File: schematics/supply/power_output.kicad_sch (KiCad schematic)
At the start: 39 parts, among them Q10 IRLML5203, U2 EL817, U22 TL331, U23 INA228, U9 IRS2153S

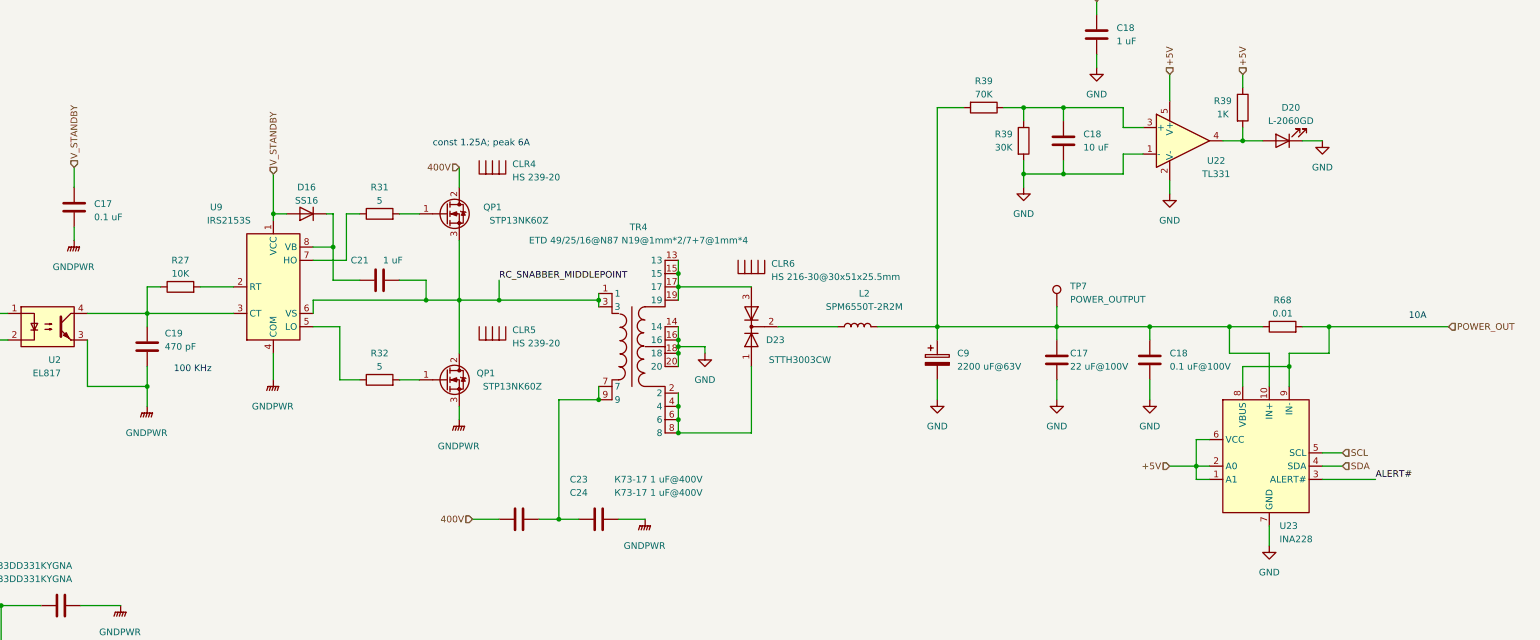
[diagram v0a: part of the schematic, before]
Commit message: prepare to replace ina228 to attiny16+ina169(?). ina228 is an intresting chip, but its too expensive and Im not sure I can buy it on ali
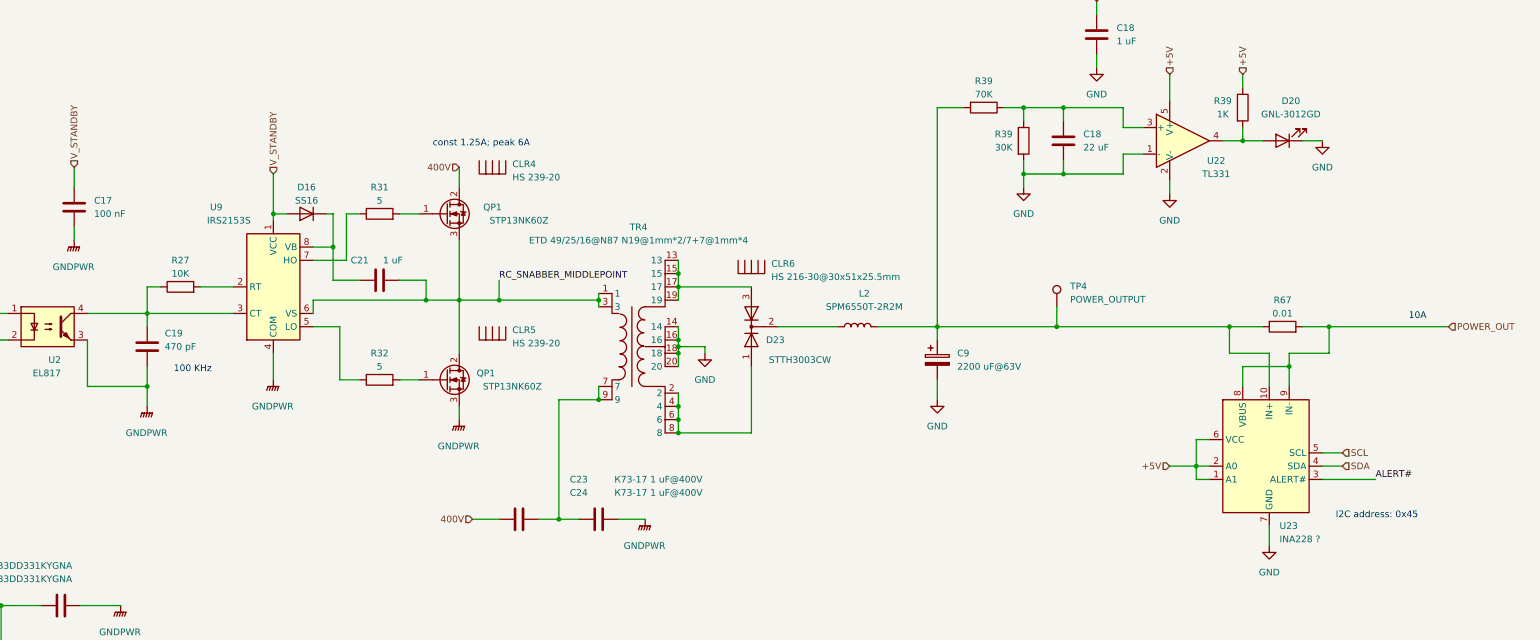
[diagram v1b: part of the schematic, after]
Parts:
- removed C17: 22 uF@100V, Capacitor_SMD:C_1210_3225Metric, symbol Device:C
- removed C18: 0.1 uF@100V, Capacitor_SMD:C_0603_1608Metric, symbol Device:C
- C17: value 0.1 uF -> 100 nF
- C18: value 10 uF -> 22 uF; footprint Capacitor_SMD:C_0603_1608Metric -> Capacitor_SMD:C_1210_3225Metric
- C23, C24: footprint Capacitor_THT:C_Rect_L31.5mm_W9.0mm_P27.50mm_MKS4 -> Capacitor_THT:C_Rect_L24.0mm_W12.8mm_P22.50mm_MKT
- D20: value L-2060GD -> GNL-3012GD
- U23: value INA228 -> INA228 ?
- renumbered R68 to R67, TP7 to TP4
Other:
- note added: "I2C address: 0x45"

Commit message: Prepare to move USB ports to a few millimenters outside
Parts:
- removed Q10 (x2): IRLML5203, Package_TO_SOT_SMD:SOT-23, symbol Transistor_FET:IRLML5203
- removed R27: 10K, Resistor_SMD:R_0805_2012Metric, symbol Device:R
- removed U23: INA228 ?, Package_SO:VSSOP-10_3x3mm_P0.5mm, symbol My_Library:INA228
- added C18 (x2): 10 nF, Capacitor_SMD:C_0603_1608Metric, symbol Device:C
- added C18: 1 uF, Capacitor_SMD:C_0603_1608Metric, symbol Device:C
- added Q10: IRLML0030, Package_TO_SOT_SMD:SOT-23, symbol Transistor_FET:IRLML0030
- added R70: 9K1, Resistor_SMD:R_0805_2012Metric, symbol Device:R
- added R71: 1K, Resistor_SMD:R_0805_2012Metric, symbol Device:R
- added R74: 49K5, Resistor_SMD:R_0805_2012Metric, symbol Device:R
- added U24: INA169, Package_TO_SOT_SMD:SOT-23-5, symbol Amplifier_Current:INA169
- R73: renamed from R67; footprint Resistor_SMD:R_1206_3216Metric -> Resistor_SMD:R_2512_6332Metric
- renumbered D20 to D23, U22 to U23
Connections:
- net +5V: now also R18.1, C18.2, U24.5 (V+)
- net GND: now also C18.1, C18.1, C18.1, Q10.2 (S), R71.1, R74.1, U24.2 (GND); no longer R18.1
- net POWER_OUT: now also U24.4 (-)
- net at R18.2: now also U2.1; no longer U2.2
- net at C9.1, L2.2, R39.2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: now also R70.2, U24.3 (+)
- new net: Q10.3 (D), U2.2
- new net POWER_OUTPUT_CURRENT_SENSE: C18.2, R74.2, U24.1
- new net POWER_OUTPUT_FB: Q10.1 (G)
- new net POWER_OUTPUT_VOLT_SENSE: C18.2, R70.1, R71.2
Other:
- note removed: "I2C address: 0x45"
- moved on the sheet: R18, R73

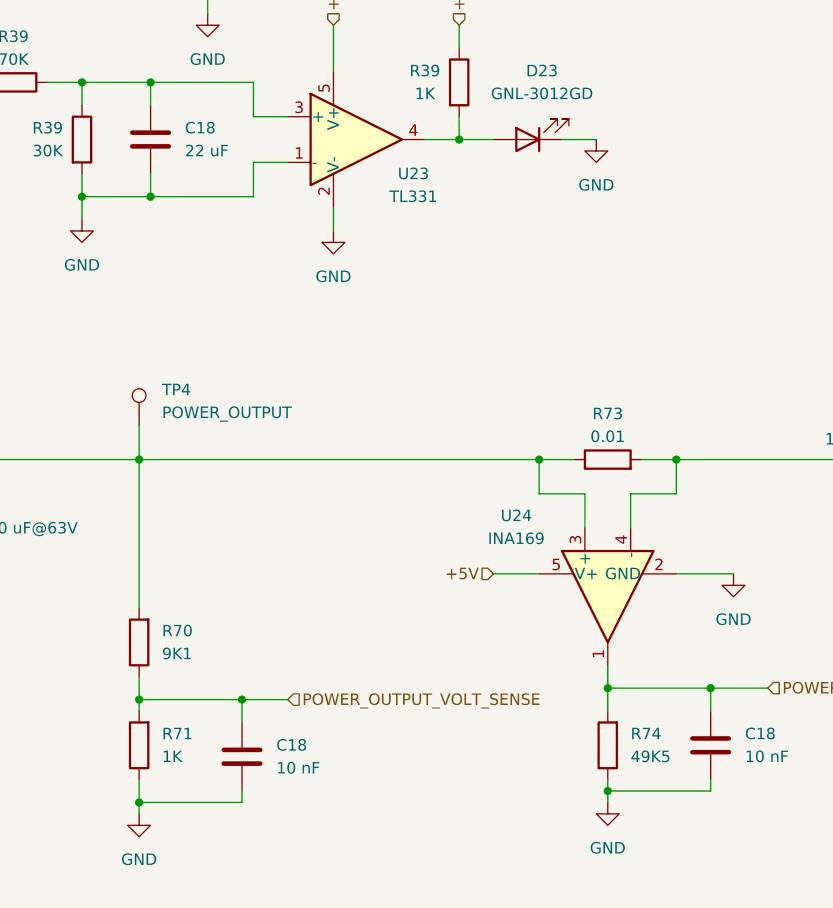
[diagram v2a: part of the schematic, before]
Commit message: little changes in schematics
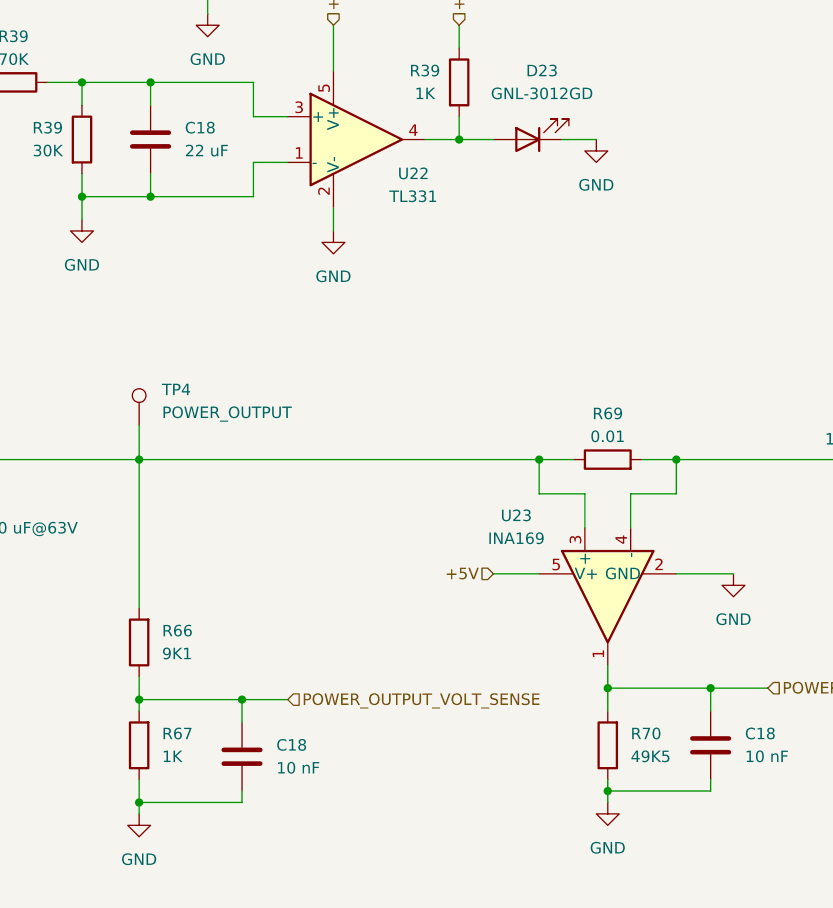
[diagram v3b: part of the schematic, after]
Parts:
- renumbered R70 to R66, R71 to R67, R73 to R69, R74 to R70, U23 to U22, U24 to U23

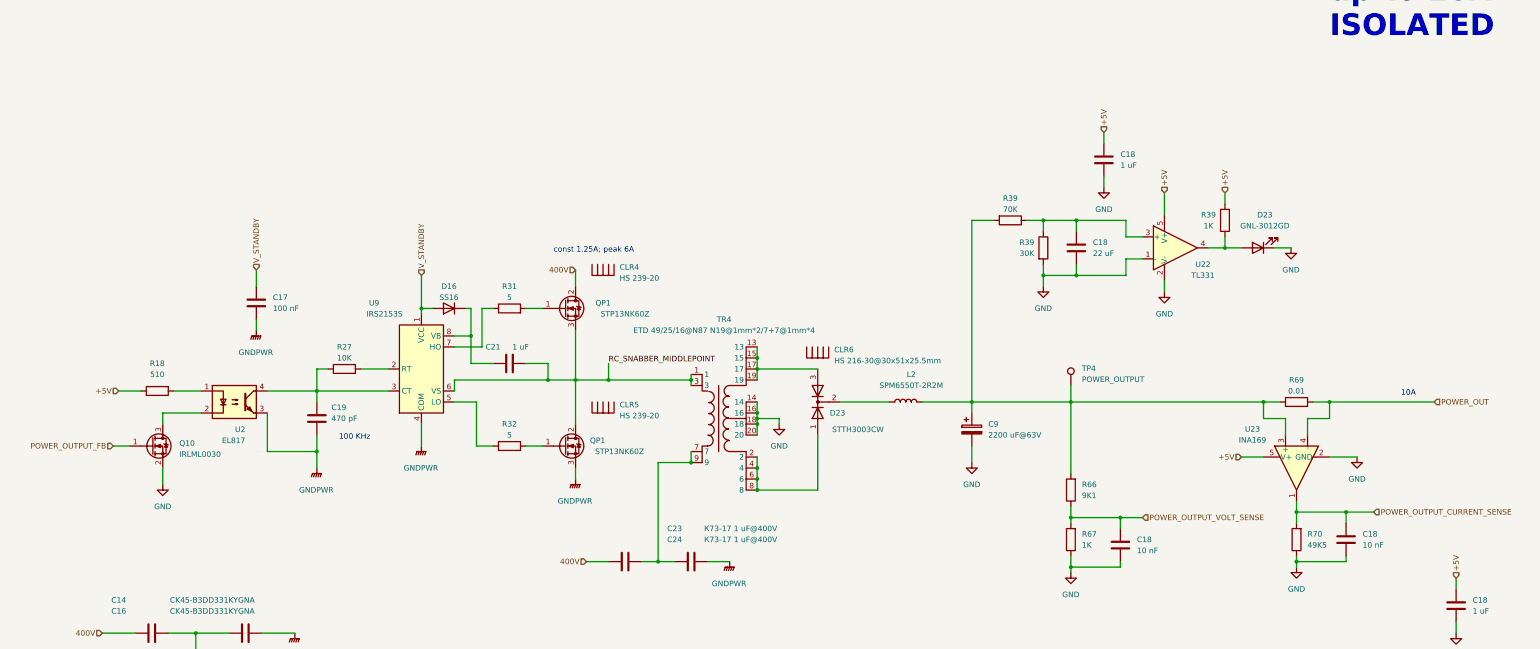
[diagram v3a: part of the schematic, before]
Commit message: Added over-voltage protection to 5V line
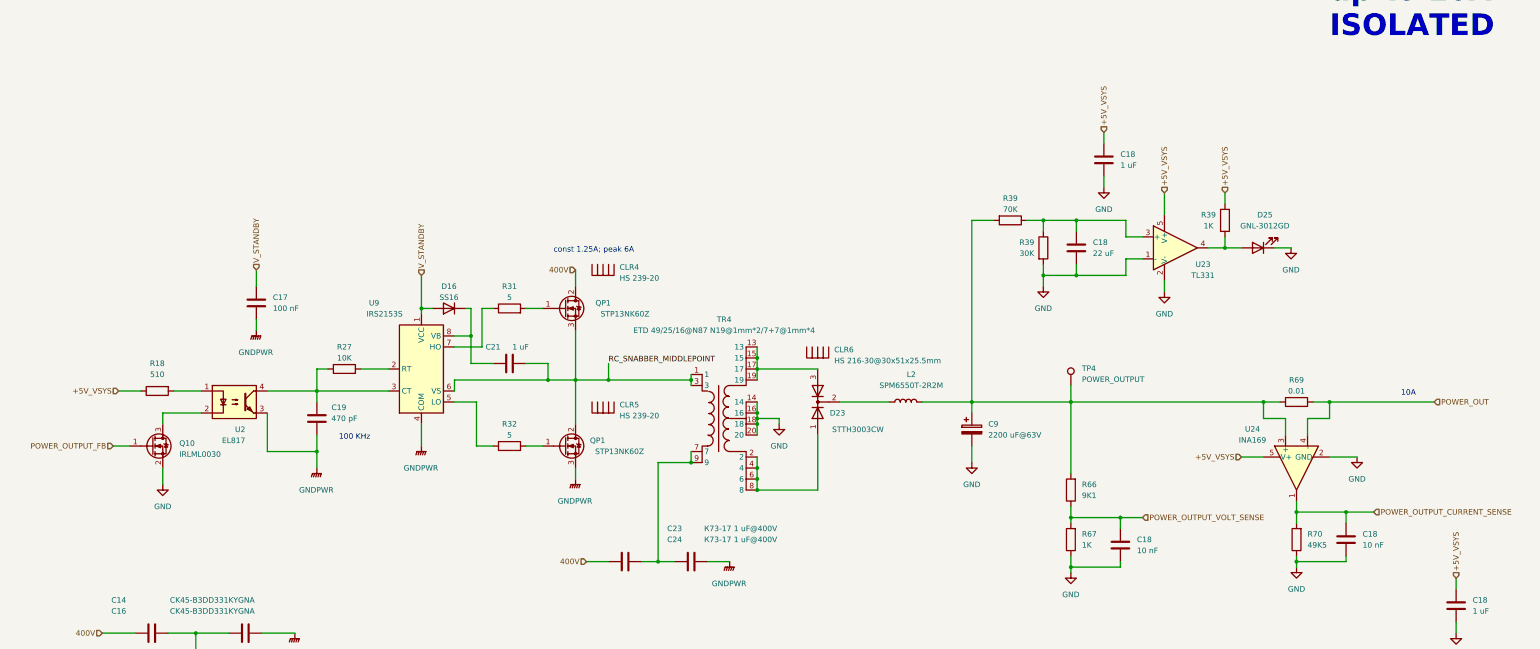
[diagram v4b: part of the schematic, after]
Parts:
- renumbered D23 to D25, U22 to U23, U23 to U24
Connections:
- net +5V renamed +5V_VSYS
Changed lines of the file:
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@@
     (effects (font (size 1.27 1.27)) (justify left))
   )
-  (hierarchical_label "+5V" (shape input) (at 327.66 87.63 90) (fields_autoplaced)
+  (hierarchical_label "+5V_VSYS" (shape input) (at 327.66 87.63 90) (fields_autoplaced)
     (effects (font (size 1.27 1.27)) (justify left))
   )
@@
     (effects (font (size 1.27 1.27)) (justify right))
   )
-  (hierarchical_label "+5V" (shape input) (at 345.44 148.59 180) (fields_autoplaced)
+  (hierarchical_label "+5V_VSYS" (shape input) (at 345.44 148.59 180) (fields_autoplaced)
     (effects (font (size 1.27 1.27)) (justify right))
   )
-  (hierarchical_label "+5V" (shape input) (at 313.69 73.66 90) (fields_autoplaced)
+  (hierarchical_label "+5V_VSYS" (shape input) (at 313.69 73.66 90) (fields_autoplaced)
     (effects (font (size 1.27 1.27)) (justify left))
   )
@@
     (effects (font (size 1.27 1.27)) (justify left))
   )
-  (hierarchical_label "+5V" (shape input) (at 341.63 87.63 90) (fields_autoplaced)
+  (hierarchical_label "+5V_VSYS" (shape input) (at 341.63 87.63 90) (fields_autoplaced)
     (effects (font (size 1.27 1.27)) (justify left))
   )
-  (hierarchical_label "+5V" (shape input) (at 86.36 133.35 180) (fields_autoplaced)
+  (hierarchical_label "+5V_VSYS" (shape input) (at 86.36 133.35 180) (fields_autoplaced)
     (effects (font (size 1.27 1.27)) (justify right))
   )
-  (hierarchical_label "+5V" (shape input) (at 394.97 176.53 90) (fields_autoplaced)
+  (hierarchical_label "+5V_VSYS" (shape input) (at 394.97 176.53 90) (fields_autoplaced)
     (effects (font (size 1.27 1.27)) (justify left))
   )
@@
         )
         (path "/1e139717-fcd1-4008-a6ea-4c993845e928/4671650e-ec71-47e3-a051-fc2ad6d25f63"
-          (reference "#PWR080") (unit 1)
+          (reference "#PWR084") (unit 1)
         )
       )
@@
         )
         (path "/1e139717-fcd1-4008-a6ea-4c993845e928/4671650e-ec71-47e3-a051-fc2ad6d25f63"
-          (reference "#PWR083") (unit 1)
+          (reference "#PWR087") (unit 1)
         )
       )
@@
         )
         (path "/1e139717-fcd1-4008-a6ea-4c993845e928/4671650e-ec71-47e3-a051-fc2ad6d25f63"
-          (reference "U21") (unit 1)
+          (reference "U22") (unit 1)
         )
       )
@@
         )
         (path "/1e139717-fcd1-4008-a6ea-4c993845e928/4671650e-ec71-47e3-a051-fc2ad6d25f63"
-          (reference "#PWR073") (unit 1)
+          (reference "#PWR077") (unit 1)
         )
       )
@@
         )
         (path "/1e139717-fcd1-4008-a6ea-4c993845e928/4671650e-ec71-47e3-a051-fc2ad6d25f63"
-          (reference "#PWR074") (unit 1)
+          (reference "#PWR078") (unit 1)
         )
       )
@@
         )
         (path "/1e139717-fcd1-4008-a6ea-4c993845e928/4671650e-ec71-47e3-a051-fc2ad6d25f63"
-          (reference "#PWR086") (unit 1)
+          (reference "#PWR090") (unit 1)
         )
       )
@@
         )
         (path "/1e139717-fcd1-4008-a6ea-4c993845e928/4671650e-ec71-47e3-a051-fc2ad6d25f63"
-          (reference "#PWR081") (unit 1)
+          (reference "#PWR085") (unit 1)
         )
       )
@@
         )
         (path "/1e139717-fcd1-4008-a6ea-4c993845e928/4671650e-ec71-47e3-a051-fc2ad6d25f63"
-          (reference "#PWR082") (unit 1)
+          (reference "#PWR086") (unit 1)
         )
       )
@@
         )
         (path "/1e139717-fcd1-4008-a6ea-4c993845e928/4671650e-ec71-47e3-a051-fc2ad6d25f63"
-          (reference "#PWR078") (unit 1)
+          (reference "#PWR082") (unit 1)
         )
       )
@@
         )
         (path "/1e139717-fcd1-4008-a6ea-4c993845e928/4671650e-ec71-47e3-a051-fc2ad6d25f63"
-          (reference "U20") (unit 1)
+          (reference "U21") (unit 1)
         )
       )
@@
         )
         (path "/1e139717-fcd1-4008-a6ea-4c993845e928/4671650e-ec71-47e3-a051-fc2ad6d25f63"
-          (reference "#PWR084") (unit 1)
+          (reference "#PWR088") (unit 1)
         )
       )
@@
         )
         (path "/1e139717-fcd1-4008-a6ea-4c993845e928/4671650e-ec71-47e3-a051-fc2ad6d25f63"
-          (reference "D21") (unit 1)
+          (reference "D23") (unit 1)
         )
       )
@@
         )
         (path "/1e139717-fcd1-4008-a6ea-4c993845e928/4671650e-ec71-47e3-a051-fc2ad6d25f63"
-          (reference "#PWR079") (unit 1)
+          (reference "#PWR083") (unit 1)
         )
       )
@@
   (symbol (lib_id "Amplifier_Current:INA169") (at 358.14 151.13 90) (mirror x) (unit 1)
     (in_bom yes) (on_board yes) (dnp no)
-    (property "Reference" "U23" (at 347.98 142.1383 90)
+    (property "Reference" "U24" (at 347.98 142.1383 90)
       (effects (font (size 1.27 1.27)))
     )
@@
       (project "supply"
         (path "/1e139717-fcd1-4008-a6ea-4c993845e928/4671650e-ec71-47e3-a051-fc2ad6d25f63"
-          (reference "U23") (unit 1)
+          (reference "U24") (unit 1)
         )
       )
@@
   (symbol (lib_id "Comparator:TL331") (at 330.2 100.33 0) (unit 1)
     (in_bom yes) (on_board yes) (dnp no)
-    (property "Reference" "U22" (at 336.55 104.14 0)
+    (property "Reference" "U23" (at 336.55 104.14 0)
       (effects (font (size 1.27 1.27)))
     )
@@
       (project "supply"
         (path "/1e139717-fcd1-4008-a6ea-4c993845e928/4671650e-ec71-47e3-a051-fc2ad6d25f63"
-          (reference "U22") (unit 1)
+          (reference "U23") (unit 1)
         )
       )
@@
         )
         (path "/1e139717-fcd1-4008-a6ea-4c993845e928/4671650e-ec71-47e3-a051-fc2ad6d25f63"
-          (reference "#PWR085") (unit 1)
+          (reference "#PWR089") (unit 1)
         )
       )
@@
   (symbol (lib_id "Device:LED") (at 349.25 100.33 180) (unit 1)
     (in_bom yes) (on_board yes) (dnp no) (fields_autoplaced)
-    (property "Reference" "D23" (at 350.8375 92.71 0)
+    (property "Reference" "D25" (at 350.8375 92.71 0)
       (effects (font (size 1.27 1.27)))
     )
@@
       (project "supply"
         (path "/1e139717-fcd1-4008-a6ea-4c993845e928/4671650e-ec71-47e3-a051-fc2ad6d25f63"
-          (reference "D23") (unit 1)
+          (reference "D25") (unit 1)
         )
       )
@@
         )
         (path "/1e139717-fcd1-4008-a6ea-4c993845e928/4671650e-ec71-47e3-a051-fc2ad6d25f63"
-          (reference "#PWR087") (unit 1)
+          (reference "#PWR091") (unit 1)
         )
       )
@@
         )
         (path "/1e139717-fcd1-4008-a6ea-4c993845e928/4671650e-ec71-47e3-a051-fc2ad6d25f63"
-          (reference "#PWR076") (unit 1)
+          (reference "#PWR080") (unit 1)
         )
       )
@@
         )
         (path "/1e139717-fcd1-4008-a6ea-4c993845e928/4671650e-ec71-47e3-a051-fc2ad6d25f63"
-          (reference "#PWR088") (unit 1)
+          (reference "#PWR092") (unit 1)
         )
       )
@@
         )
         (path "/1e139717-fcd1-4008-a6ea-4c993845e928/4671650e-ec71-47e3-a051-fc2ad6d25f63"
-          (reference "#PWR075") (unit 1)
+          (reference "#PWR079") (unit 1)
         )
       )
@@
         )
         (path "/1e139717-fcd1-4008-a6ea-4c993845e928/4671650e-ec71-47e3-a051-fc2ad6d25f63"
-          (reference "#PWR077") (unit 1)
+          (reference "#PWR081") (unit 1)
         )
       )
@@
         )
         (path "/1e139717-fcd1-4008-a6ea-4c993845e928/4671650e-ec71-47e3-a051-fc2ad6d25f63"
-          (reference "#PWR089") (unit 1)
+          (reference "#PWR093") (unit 1)
         )
       )
@@
         )
         (path "/1e139717-fcd1-4008-a6ea-4c993845e928/4671650e-ec71-47e3-a051-fc2ad6d25f63"
-          (reference "D22") (unit 1)
-        )
-      )
+          (reference "D24") (unit 1)
+        )
+      )
